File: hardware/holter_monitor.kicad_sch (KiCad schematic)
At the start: 52 parts, among them J1 USB_C_Receptacle_USB2.0_16P, J2 BAT JST-PH, J3 AD8232, J4 UART, Q1 AO3401A, SW1 SW_SPDT, SW2 RESET, SW3 BOOT, U1 USBLC6-2SC6, U2 MCP73831-2-OT, U3 AP2112K-3.3, U4 ESP32-S3-WROOM-1

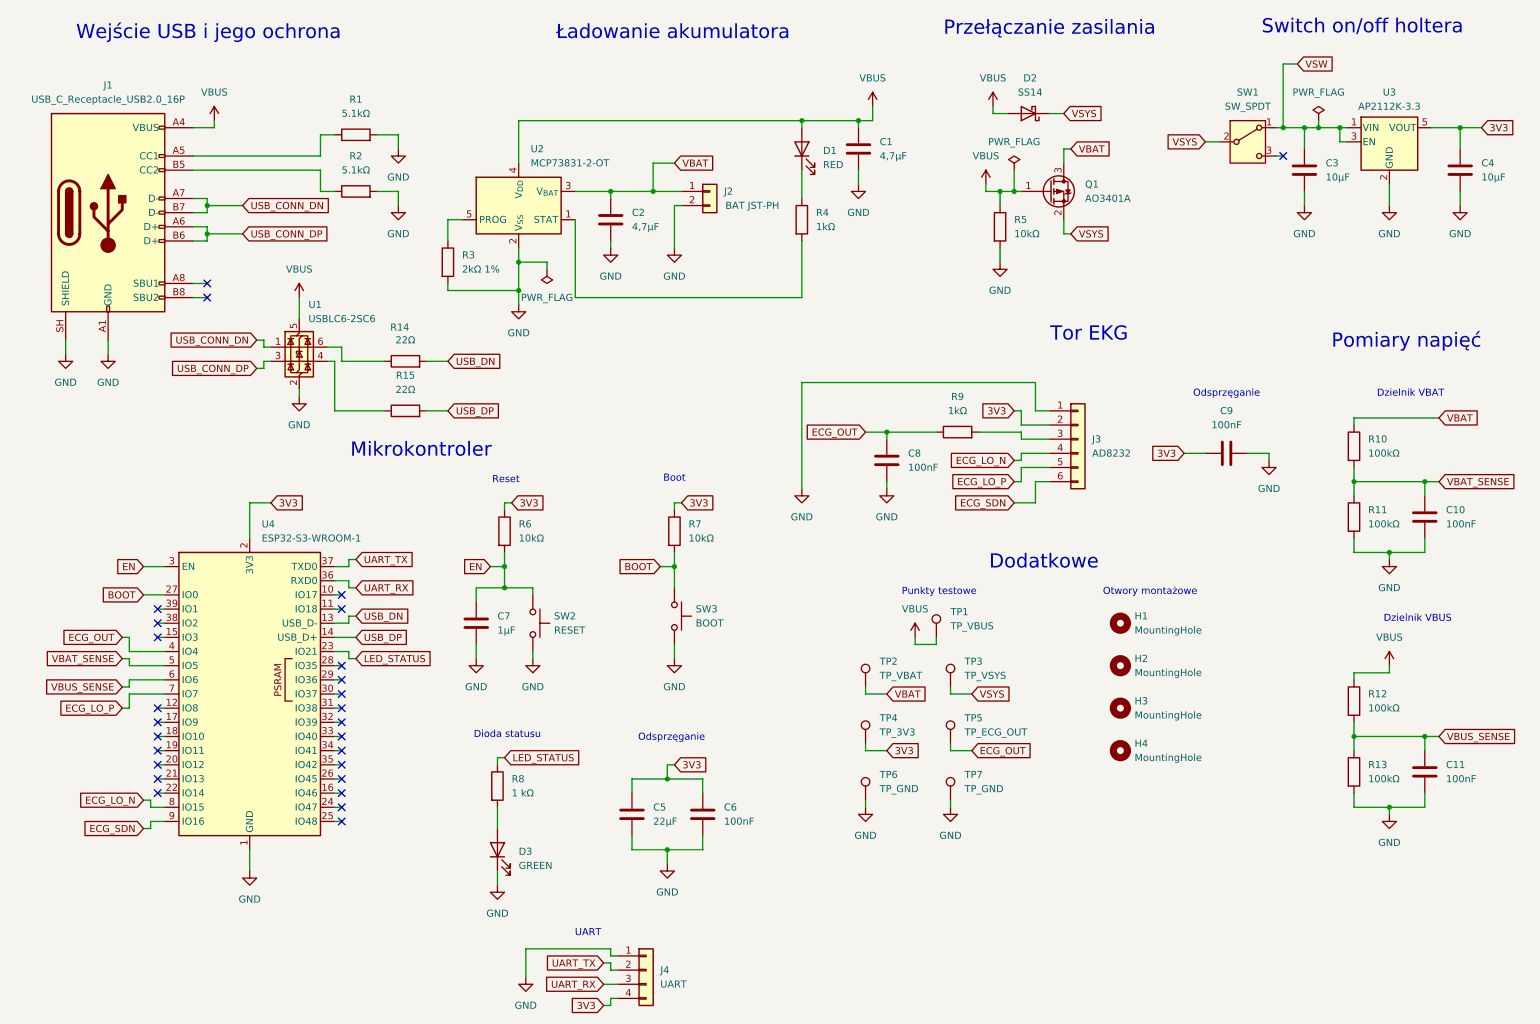
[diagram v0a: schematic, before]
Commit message: Switched from just the AD8232 symbol to full SEN-12650 module symbol
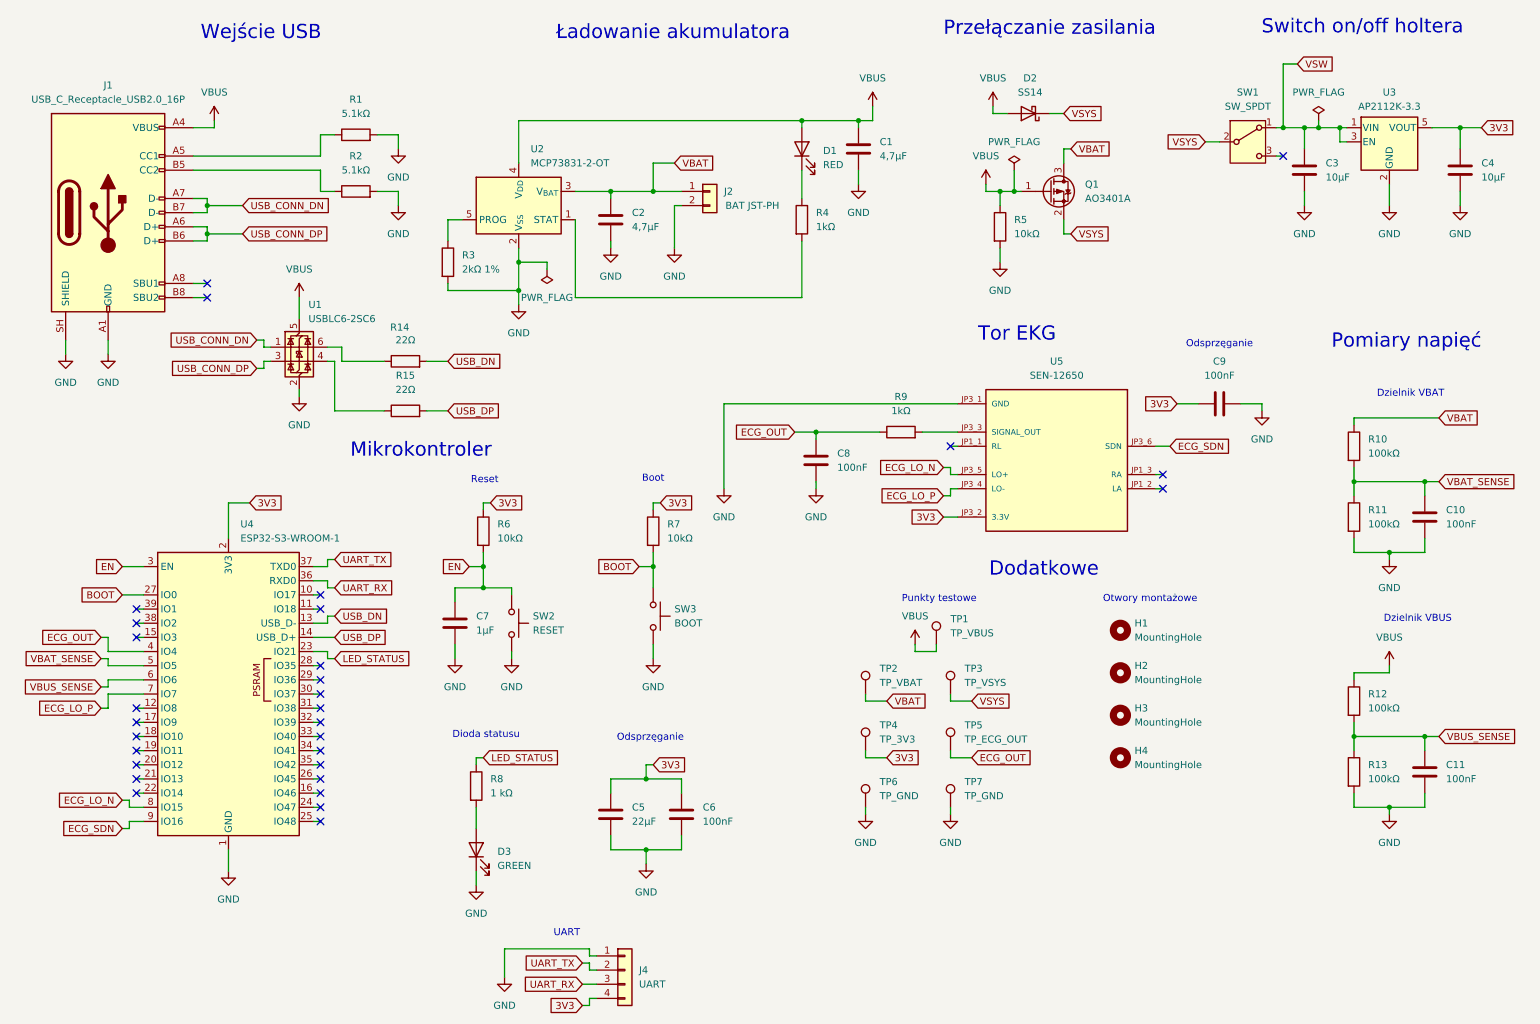
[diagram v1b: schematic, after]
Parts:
- removed J3: AD8232, Connector_PinSocket_2.54mm:PinSocket_1x06_P2.54mm_Vertical, symbol Connector_Generic:Conn_01x06
- added U5: SEN-12650, SEN-12650:MODULE_SEN-12650, symbol SEN-12650:SEN-12650
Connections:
- net 3V3: now also U5.JP3_2 (3.3V)
- net ECG_LO_N: now also U5.JP3_5 (LO+)
- net ECG_LO_P: now also U5.JP3_4 (LO-)
- net ECG_SDN: now also U5.JP3_6 (SDN)
- net GND: now also U5.JP3_1 (GND)
- net at R9.2: now also U5.JP3_3 (SIGNAL_OUT)
- no-connect marks 27 -> 30
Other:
- note added: "Wejście USB"
- note removed: "Wejście USB i jego ochrona"
- moved on the sheet: C5, C6, C7, C8, C9, D3, H1, H2, H3, H4, J4, R6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

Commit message: Switched from AD8232 footprint to complete SEN-12650 module footprint
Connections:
- net ECG_LO_N: now also U5.JP3_4 (LO-); no longer U5.JP3_5 (LO+)
- net ECG_LO_P: now also U5.JP3_5 (LO+); no longer U5.JP3_4 (LO-)

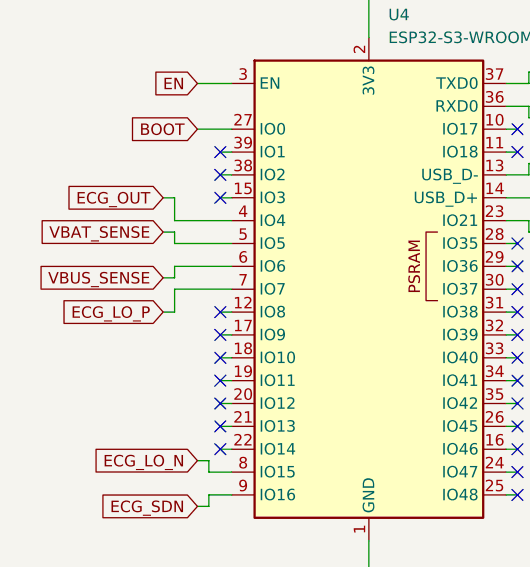
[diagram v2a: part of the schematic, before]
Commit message: Switched VBAT and VBUS SENSE labels in ESP32-S3 from IO5/6 to IO9/10 to have more space
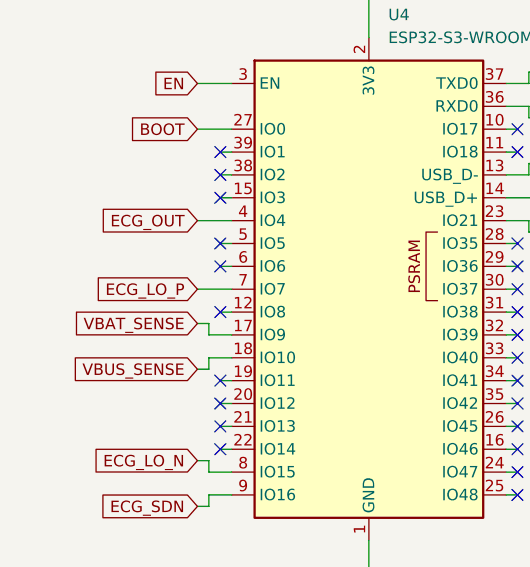
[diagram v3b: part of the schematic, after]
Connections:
- net VBAT_SENSE: now also U4.17 (IO9); no longer U4.5 (IO5)
- net VBUS_SENSE: now also U4.18 (IO10); no longer U4.6 (IO6)
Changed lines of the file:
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@@
 	)
 	(no_connect
+		(at 34.29 134.62)
+	)
+	(no_connect
 		(at 67.31 154.94)
 	)
@@
 	)
 	(no_connect
-		(at 218.44 100.33)
+		(at 34.29 132.08)
 	)
 	(no_connect
-		(at 34.29 144.78)
+		(at 218.44 100.33)
 	)
 	(no_connect
@@
 	)
 	(no_connect
-		(at 34.29 142.24)
-	)
-	(no_connect
 		(at 218.44 97.79)
 	)
@@
 	(wire
 		(pts
-			(xy 29.21 132.08) (xy 29.21 130.81)
-		)
-		(stroke
-			(width 0)
-			(type default)
-		)
-	)
-	(wire
-		(pts
-			(xy 27.94 135.89) (xy 29.21 135.89)
-		)
-		(stroke
-			(width 0)
-			(type default)
-		)
-	)
-	(wire
-		(pts
-			(xy 29.21 134.62) (xy 35.56 134.62)
+			(xy 33.02 144.78) (xy 33.02 146.05)
 		)
 		(stroke
@@
 	(wire
 		(pts
+			(xy 31.75 140.97) (xy 33.02 140.97)
+		)
+		(stroke
+			(width 0)
+			(type default)
+		)
+	)
+	(wire
+		(pts
 			(xy 92.71 52.07) (xy 90.17 52.07)
 		)
@@
 	(wire
 		(pts
-			(xy 29.21 129.54) (xy 29.21 127)
+			(xy 35.56 157.48) (xy 33.02 157.48)
 		)
 		(stroke
@@
 	(wire
 		(pts
-			(xy 35.56 157.48) (xy 33.02 157.48)
+			(xy 265.43 144.78) (xy 265.43 147.32)
 		)
 		(stroke
@@
 	(wire
 		(pts
-			(xy 265.43 144.78) (xy 265.43 147.32)
+			(xy 81.28 46.99) (xy 81.28 49.53)
 		)
 		(stroke
@@
 	(wire
 		(pts
-			(xy 81.28 46.99) (xy 81.28 49.53)
+			(xy 33.02 142.24) (xy 33.02 140.97)
 		)
 		(stroke
@@
 	(wire
 		(pts
-			(xy 27.94 127) (xy 29.21 127)
-		)
-		(stroke
-			(width 0)
-			(type default)
-		)
-	)
-	(wire
-		(pts
 			(xy 180.34 137.16) (xy 180.34 138.43)
 		)
@@
 	(wire
 		(pts
-			(xy 34.29 142.24) (xy 35.56 142.24)
+			(xy 34.29 132.08) (xy 35.56 132.08)
 		)
 		(stroke
@@
 	(wire
 		(pts
-			(xy 29.21 137.16) (xy 35.56 137.16)
-		)
-		(stroke
-			(width 0)
-			(type default)
-		)
-	)
-	(wire
-		(pts
 			(xy 102.87 64.77) (xy 102.87 67.31)
 		)
@@
 	(wire
 		(pts
-			(xy 27.94 139.7) (xy 29.21 139.7)
+			(xy 31.75 137.16) (xy 35.56 137.16)
+		)
+		(stroke
+			(width 0)
+			(type default)
+		)
+	)
+	(wire
+		(pts
+			(xy 34.29 134.62) (xy 35.56 134.62)
 		)
 		(stroke
@@
 	(wire
 		(pts
+			(xy 31.75 129.54) (xy 35.56 129.54)
+		)
+		(stroke
+			(width 0)
+			(type default)
+		)
+	)
+	(wire
+		(pts
 			(xy 113.03 66.04) (xy 153.67 66.04)
 		)
@@
 	(wire
 		(pts
+			(xy 33.02 142.24) (xy 35.56 142.24)
+		)
+		(stroke
+			(width 0)
+			(type default)
+		)
+	)
+	(wire
+		(pts
 			(xy 219.71 92.71) (xy 217.17 92.71)
 		)
@@
 	(wire
 		(pts
-			(xy 179.07 96.52) (xy 180.34 96.52)
+			(xy 31.75 146.05) (xy 33.02 146.05)
 		)
 		(stroke
@@
 	(wire
 		(pts
-			(xy 34.29 152.4) (xy 35.56 152.4)
+			(xy 33.02 144.78) (xy 35.56 144.78)
 		)
 		(stroke
@@
 	(wire
 		(pts
-			(xy 50.8 165.1) (xy 50.8 168.91)
+			(xy 179.07 96.52) (xy 180.34 96.52)
 		)
 		(stroke
@@
 	(wire
 		(pts
-			(xy 27.94 130.81) (xy 29.21 130.81)
+			(xy 34.29 152.4) (xy 35.56 152.4)
+		)
+		(stroke
+			(width 0)
+			(type default)
+		)
+	)
+	(wire
+		(pts
+			(xy 50.8 165.1) (xy 50.8 168.91)
 		)
 		(stroke
@@
 	(wire
 		(pts
-			(xy 29.21 134.62) (xy 29.21 135.89)
-		)
-		(stroke
-			(width 0)
-			(type default)
-		)
-	)
-	(wire
-		(pts
 			(xy 259.08 132.08) (xy 259.08 133.35)
 		)
@@
 	(wire
 		(pts
-			(xy 29.21 129.54) (xy 35.56 129.54)
-		)
-		(stroke
-			(width 0)
-			(type default)
-		)
-	)
-	(wire
-		(pts
 			(xy 66.04 152.4) (xy 67.31 152.4)
 		)
@@
 	(wire
 		(pts
-			(xy 34.29 144.78) (xy 35.56 144.78)
-		)
-		(stroke
-			(width 0)
-			(type default)
-		)
-	)
-	(wire
-		(pts
 			(xy 177.8 129.54) (xy 173.99 129.54)
 		)
@@
 	(wire
 		(pts
-			(xy 29.21 137.16) (xy 29.21 139.7)
-		)
-		(stroke
-			(width 0)
-			(type default)
-		)
-	)
-	(wire
-		(pts
 			(xy 243.84 35.56) (xy 243.84 39.37)
 		)
@@
 	(wire
 		(pts
-			(xy 29.21 132.08) (xy 35.56 132.08)
-		)
-		(stroke
-			(width 0)
-			(type default)
-		)
-	)
-	(wire
-		(pts
 			(xy 46.99 49.53) (xy 46.99 50.8)
 		)
@@
 	(global_label "VBAT_SENSE"
 		(shape input)
-		(at 27.94 130.81 180)
+		(at 31.75 140.97 180)
 		(fields_autoplaced yes)
 		(effects
@@
 		)
 		(property "Intersheetrefs" "${INTERSHEET_REFS}"
-			(at 13.5249 130.81 0)
+			(at 17.3349 140.97 0)
 			(hide yes)
 			(show_name no)
@@
 	(global_label "ECG_LO_P"
 		(shape input)
-		(at 27.94 139.7 180)
+		(at 31.75 137.16 180)
 		(fields_autoplaced yes)
 		(effects
@@
 		)
 		(property "Intersheetrefs" "${INTERSHEET_REFS}"
-			(at 15.702 139.7 0)
+			(at 19.512 137.16 0)
 			(hide yes)
 			(show_name no)
@@
 	(global_label "ECG_OUT"
 		(shape input)
-		(at 27.94 127 180)
+		(at 31.75 129.54 180)
 		(fields_autoplaced yes)
 		(effects
@@
 		)
 		(property "Intersheetrefs" "${INTERSHEET_REFS}"
-			(at 16.6696 127 0)
+			(at 20.4796 129.54 0)
 			(hide yes)
 			(show_name no)
@@
 	(global_label "VBUS_SENSE"
 		(shape input)
-		(at 27.94 135.89 180)
+		(at 31.75 146.05 180)
 		(fields_autoplaced yes)
 		(effects
@@
 		)
 		(property "Intersheetrefs" "${INTERSHEET_REFS}"
-			(at 13.0411 135.89 0)
+			(at 16.8511 146.05 0)
 			(hide yes)
 			(show_name no)
